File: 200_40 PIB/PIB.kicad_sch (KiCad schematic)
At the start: 171 parts, among them J1 M80-5100442, J11 53398-0271, J12 M80-5100842, J13 53398-0271, J15 53398-0571, J2 53398-0471, J3 G125-MS12605M2P, J5 53398-1371, J8 SWD/DEBUG, Q1 Si7489DP, Q11 IRF7832, Q2 Si7489DP, Q9 IRF7832, SW1 SKRKAHE020, U10 LT8580EDD, U12 MAX823TEUK_T, U14 74HC08PW, U15 74HC08PW, U4 STM32G431RBTx, U5 ADM1270ACPZ, U7 ADM1270ACPZ, U8 74AHC1G125, Y1 ABM3B-8.000MHZ-10-D1G-T

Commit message: lots of claude close outs
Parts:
- removed C21, C28, C32, C33, C66, C67: 1uF, Capacitor_SMD:C_0603_1608Metric, symbol Device:C
- removed C29, C34: 100nF, Capacitor_SMD:C_0402_1005Metric, symbol Device:C
- removed C30, C35: 10nF, Capacitor_SMD:C_0402_1005Metric, symbol Device:C
- removed Q1, Q2: Si7489DP, Package_SO:PowerPAK_SO-8_Single, symbol Transistor_FET:Si7141DP
- removed R35: 15m, Resistor_SMD:R_0805_2012Metric, symbol Device:R
- removed R48, R61: 2K, Resistor_SMD:R_0402_1005Metric, symbol Device:R
- removed R49, R54, R60, R69: 1K, Resistor_SMD:R_0402_1005Metric, symbol Device:R
- removed R50, R57, R59, R66: 33K, Resistor_SMD:R_0402_1005Metric, symbol Device:R
- removed R51, R64: 0R, Resistor_SMD:R_0402_1005Metric, symbol Device:R
- removed R52, R55, R56, R58, R62, R67, R68, R70: 10K, Resistor_SMD:R_0402_1005Metric, symbol Device:R
- removed R53, R63: 100K, Resistor_SMD:R_0402_1005Metric, symbol Device:R
- removed R65: 100m, Resistor_SMD:R_0603_1608Metric, symbol Device:R
- removed U5, U7: ADM1270ACPZ, Package_CSP:LFCSP-16-1EP_3x3mm_P0.5mm_EP1.5x1.5mm, symbol Power_Management:ADM1270ACPZ
- added C78, C79, C82: 1uF, Capacitor_SMD:C_0603_1608Metric, symbol Device:C
- added C80: 100nF, Capacitor_SMD:C_0402_1005Metric, symbol Device:C
- added C81: 22nF, Capacitor_SMD:C_0402_1005Metric, symbol Device:C
- added Q6: Si7489DP, Package_SO:PowerPAK_SO-8_Single, symbol Transistor_FET:Si7141DP
- added R111: 33K, Resistor_SMD:R_0402_1005Metric, symbol Device:R
- added R112, R120: 1K, Resistor_SMD:R_0402_1005Metric, symbol Device:R
- added R113: 2K, Resistor_SMD:R_0402_1005Metric, symbol Device:R
- added R114, R118, R119, R121: 10K, Resistor_SMD:R_0402_1005Metric, symbol Device:R
- added R115, R117, R124: 100K, Resistor_SMD:R_0402_1005Metric, symbol Device:R
- added R116: 0R, Resistor_SMD:R_0402_1005Metric, symbol Device:R
- added R125: 150K, Resistor_SMD:R_0402_1005Metric, symbol Device:R
- added R38: 10m, Resistor_SMD:R_0805_2012Metric, symbol Device:R
- added U19: ADM1270ACPZ, Package_CSP:LFCSP-16-1EP_3x3mm_P0.5mm_EP1.5x1.5mm, symbol Power_Management:ADM1270ACPZ
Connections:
- net +3.3V: now also R121.2
- net GND: now also C78.2, C79.2, C80.2, C81.2, C82.2, R113.1, R115.1, R118.1, R120.1, R124.1, U19.17 (EP), U19.7 (GND)
- net 12V_PG: now reaches U4.14 (PA2)
- net BAT_EN: now reaches U4.44 (PA10)
- net BAT_EN: now also R114.1
- net BAT_PGOOD: now reaches U4.45 (PA11)
- net BAT_PGOOD: now also R121.1, U19.12 (PWRGD)
- net BAT_HOT renamed VBAT_HOT
- net VBAT_HOT: now also C79.1, R111.2, R38.2, U19.15 (VCC); no longer C62.1, J2.2 (Pin_2), J2.3 (Pin_3)
- new net: R119.1, R120.2, U19.10 (FB_PG)
- new net: R117.1, R118.2, U19.11 (FLB)
- new net: R112.1, R113.2, U19.4 (OV)
- new net: R111.1, R112.2, U19.3 (UV)
- new net: R114.2, R115.2, R116.1, U19.5 (ENABLE)
- new net: C81.1, U19.8 (TIMER)
- new net: R124.2, R125.1, U19.2 (ISET)
- new net: C78.1, R125.2, U19.1 (VCAP)
- new net: R116.2, U19.6 (~{FAULT})
- new net: Q6.1 (S), Q6.2 (S), Q6.3 (S), R38.1, U19.14 (SENSE-)
- new net: Q6.4 (G), U19.13 (GATE)
- new net: C80.1, U19.9 (TIMER_OFF)
- new net VBAT_PROT: C62.1, C82.1, J2.2 (Pin_2), J2.3 (Pin_3), Q6.5 (D), R117.2, R119.2
- no-connect marks 5 -> 4
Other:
- added sheet Discharge Load Switch (Discharge Load Switch.kicad_sch)
- added sheet Igniter Load Switch (Igniter Load Switch.kicad_sch)
- sheet Valve Driver ports: added 12V_PG; removed none
- note added: "3.6A OCP"
- note removed: "3.33A OCP"
- note removed: "500mA OCP"
- moved on the sheet: C25, C44, C63, C64, C65, D12, D15, D16, D24, D25, D26, D27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

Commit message: correct 3d model paths
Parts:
- removed Q6: Si7489DP, Package_SO:PowerPAK_SO-8_Single, symbol Transistor_FET:Si7141DP
- added Q6: Si7489DP, 0_PAY_Footprint_Library:PowerPAK_SO-8_Single, symbol 0_PAY_Symbol_Library:Si7489DP
- J3: footprint Connector_Harwin:Harwin_Gecko_G125-MS12605M2P_2x13_P1.25mm_Vertical -> 0_PAY_Footprint_Library:Harwin_Gecko_G125-MS12605M2P_2x13_P1.25mm_Vertical
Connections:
- net VBAT_PROT: now also Q6.5 (D)
- net at R38.1, U19.14 (SENSE-): now also Q6.1 (S), Q6.2 (S), Q6.3 (S)
- net at U19.13 (GATE): now also Q6.4 (G)
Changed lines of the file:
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@@
 			)
 		)
-		(property "Footprint" "Connector_Harwin:Harwin_Gecko_G125-MS12605M2P_2x13_P1.25mm_Vertical"
+		(property "Footprint" "0_PAY_Footprint_Library:Harwin_Gecko_G125-MS12605M2P_2x13_P1.25mm_Vertical"
 			(at 44.45 44.45 0)
 			(hide yes)
@@
 	)
 	(symbol
+		(lib_id "0_PAY_Symbol_Library:Si7489DP")
+		(at 90.17 118.11 270)
+		(mirror x)
+		(unit 1)
+		(body_style 1)
+		(exclude_from_sim no)
+		(in_bom yes)
+		(on_board yes)
+		(in_pos_files yes)
+		(dnp no)
+		(property "Reference" "Q6"
+			(at 90.17 109.22 90)
+			(show_name no)
+			(do_not_autoplace no)
+			(effects
+				(font
+					(size 1.27 1.27)
+				)
+			)
+		)
+		(property "Value" "Si7489DP"
+			(at 90.17 111.76 90)
+			(show_name no)
+			(do_not_autoplace no)
+			(effects
+				(font
+					(size 1.27 1.27)
+				)
+			)
+		)
+		(property "Footprint" "0_PAY_Footprint_Library:PowerPAK_SO-8_Single"
+			(at 88.265 113.03 0)
+			(hide yes)
+			(show_name no)
+			(do_not_autoplace no)
+			(effects
+				(font
+					(size 1.27 1.27)
+					(italic yes)
+				)
+				(justify left)
+			)
+		)
+		(property "Datasheet" "https://www.vishay.com/docs/73436/si7489dp.pdf"
+			(at 86.36 113.03 0)
+			(hide yes)
+			(show_name no)
+			(do_not_autoplace no)
+			(effects
+				(font
+					(size 1.27 1.27)
+				)
+				(justify left)
+			)
+		)
+		(property "Description" "-28A Id, -100V Vds, 33mOhm Rdson"
+			(at 90.17 118.11 0)
+			(hide yes)
+			(show_name no)
+			(do_not_autoplace no)
+			(effects
+				(font
+					(size 1.27 1.27)
+				)
+			)
+		)
+		(pin "2"
+		)
+		(pin "4"
+		)
+		(pin "1"
+		)
+		(pin "3"
+		)
+		(pin "5"
+		)
+		(instances
+			(project "PIB"
+				(path "/2bb2e4a1-de70-477a-a246-143db0a21e08"
+					(reference "Q6")
+					(unit 1)
+				)
+			)
+		)
+	)
+	(symbol
 		(lib_id "Diode:SMF18A")
 		(at 377.19 92.71 270)
@@
 					(unit 1)
 				)
-			)
-		)
-	)
-	(symbol
-		(lib_id "Transistor_FET:Si7141DP")
-		(at 90.17 118.11 270)
-		(mirror x)
-		(unit 1)
-		(body_style 1)
-		(exclude_from_sim no)
-		(in_bom yes)
-		(on_board yes)
-		(in_pos_files yes)
-		(dnp no)
-		(fields_autoplaced yes)
-		(property "Reference" "Q6"
-			(at 90.17 109.22 90)
-			(show_name no)
-			(do_not_autoplace no)
-			(effects
-				(font
-					(size 1.27 1.27)
-				)
-			)
-		)
-		(property "Value" "Si7489DP"
-			(at 90.17 111.76 90)
-			(show_name no)
-			(do_not_autoplace no)
-			(effects
-				(font
-					(size 1.27 1.27)
-				)
-			)
-		)
-		(property "Footprint" "Package_SO:PowerPAK_SO-8_Single"
-			(at 88.265 113.03 0)
-			(hide yes)
-			(show_name no)
-			(do_not_autoplace no)
-			(effects
-				(font
-					(size 1.27 1.27)
-					(italic yes)
-				)
-				(justify left)
-			)
-		)
-		(property "Datasheet" "https://www.vishay.com/docs/65596/si7141dp.pdf"
-			(at 86.36 113.03 0)
-			(hide yes)
-			(show_name no)
-			(do_not_autoplace no)
-			(effects
-				(font
-					(size 1.27 1.27)
-				)
-				(justify left)
-			)
-		)
-		(property "Description" "-60A Id, -20V Vds, 1.9 mOhm Ron, PowerPAK-8"
-			(at 90.17 118.11 0)
-			(hide yes)
-			(show_name no)
-			(do_not_autoplace no)
-			(effects
-				(font
-					(size 1.27 1.27)
-				)
-			)
-		)
-		(pin "4"
-		)
-		(pin "2"
-		)
-		(pin "5"
-		)
-		(pin "1"
-		)
-		(pin "3"
-		)
-		(instances
-			(project "PIB"
-				(path "/2bb2e4a1-de70-477a-a246-143db0a21e08"
-					(reference "Q6")
-					(unit 1)
-				)

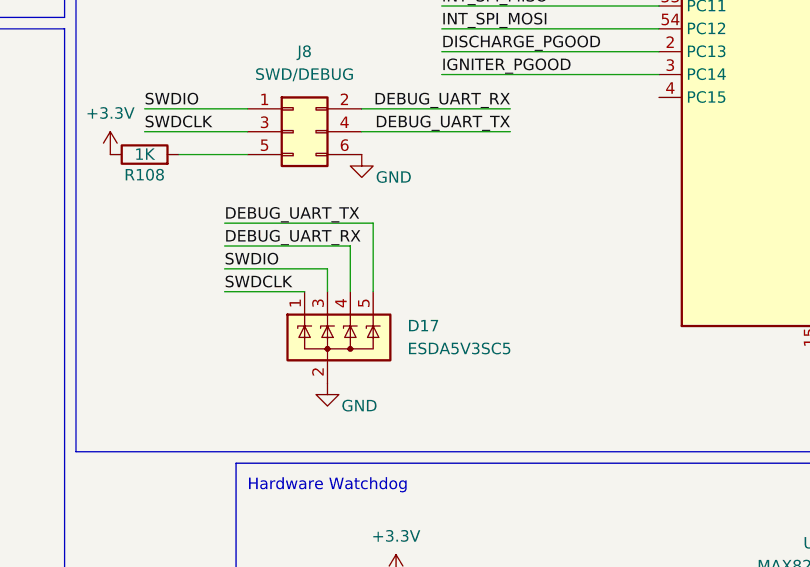
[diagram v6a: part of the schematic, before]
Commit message: finish routing with all critical schematic fixes
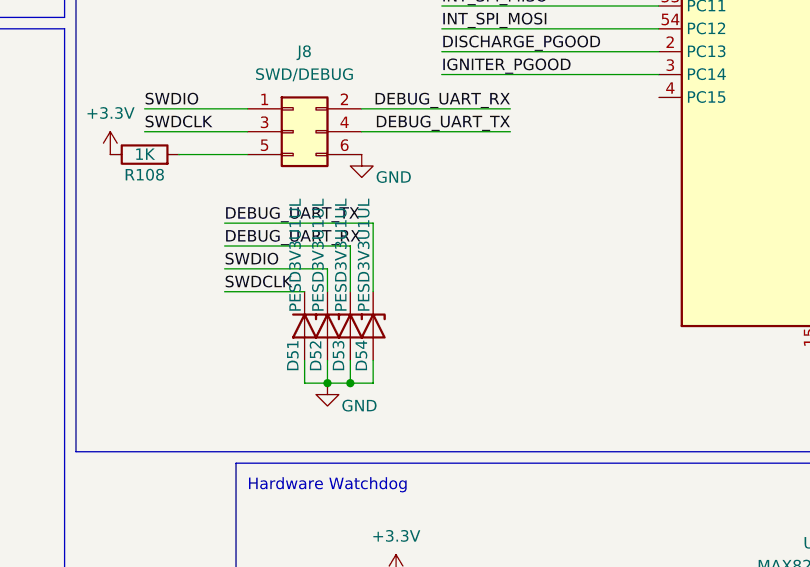
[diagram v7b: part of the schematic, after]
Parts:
- removed D17: ESDA5V3SC5, Package_TO_SOT_SMD:SOT-23-5, symbol Power_Protection:ESDA5V3SC5
- added D51, D52, D53, D54: PESD3V3U1UL, Diode_SMD:D_SOD-882, symbol Diode:PESD3V3U1UL
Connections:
- net DEBUG_UART_RX: now also D53.1 (K)
- net DEBUG_UART_TX: now also D54.1 (K)
- net GND: now also D51.2 (A), D52.2 (A), D53.2 (A), D54.2 (A)
- net SWDCLK: now also D51.1 (K)
- net SWDIO: now also D52.1 (K)

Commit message: correct V igniter and I igniter pinouts and note capacitance limits from current limit timer
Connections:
- net ADC_I_IGN_PK: now also D25.1 (K), J5.5 (Pin_5), U4.36 (PB14); no longer D24.1 (K), J5.4 (Pin_4), U4.10 (PC2)
- net ADC_V_IGN_PK: now also D24.1 (K), J5.4 (Pin_4), U4.10 (PC2); no longer D25.1 (K), J5.5 (Pin_5), U4.36 (PB14)
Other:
- note added: "235μF Worst Case Capacitance"
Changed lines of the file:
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@@
 		)
 	)
+	(text "235μF Worst Case Capacitance"
+		(exclude_from_sim no)
+		(at 147.574 123.19 0)
+		(effects
+			(font
+				(size 1.27 1.27)
+			)
+		)
+	)
 	(text "Igniter Buffer\n"
 		(exclude_from_sim no)
@@
 		)
 	)
-	(label "ADC_V_IGN_PK"
+	(label "ADC_I_IGN_PK"
 		(at 298.45 128.27 180)
 		(effects
@@
 		)
 	)
+	(label "ADC_V_IGN_PK"
+		(at 83.82 184.15 0)
+		(effects
+			(font
+				(size 1.27 1.27)
+			)
+			(justify left bottom)
+		)
+	)
 	(label "EXT_SPI_SCK"
 		(at 25.4 46.99 0)
@@
 		)
 	)
-	(label "ADC_I_IGN_PK"
+	(label "ADC_V_IGN_PK"
 		(at 222.25 77.47 0)
 		(effects
@@
 		)
 	)
-	(label "ADC_I_IGN_PK"
+	(label "ADC_V_IGN_PK"
 		(at 59.69 208.28 0)
 		(effects
@@
 		)
 	)
-	(label "ADC_I_IGN_PK"
-		(at 83.82 184.15 0)
-		(effects
-			(font
-				(size 1.27 1.27)
-			)
-			(justify left bottom)
-		)
-	)
-	(label "ADC_V_IGN_PK"
-		(at 83.82 186.69 0)
-		(effects
-			(font
-				(size 1.27 1.27)
-			)
-			(justify left bottom)
-		)
-	)
 	(label "VALVE1_L"
 		(at 298.45 100.33 180)
@@
 		)
 	)
+	(label "ADC_I_IGN_PK"
+		(at 83.82 186.69 0)
+		(effects
+			(font
+				(size 1.27 1.27)
+			)
+			(justify left bottom)
+		)
+	)
 	(label "ARM{slash}~{SAFE}"
 		(at 228.6 250.19 0)
@@
 		)
 	)
-	(label "ADC_V_IGN_PK"
+	(label "ADC_I_IGN_PK"
 		(at 59.69 205.74 0)
 		(effects
